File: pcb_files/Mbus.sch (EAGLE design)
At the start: 50 parts, among them IC1 NCP1117ST50T3G, IC3 ATMEGA2560-16AU, IC4 RTC_PCF8523T, J1 F-1X18-SIP-100-32Y, J2 USB_A_SMT_FEMALE, J3 USB_A_SMT_FEMALE, J4 USB_A_SMT_FEMALE, M1 SERVO, Q2 32.768, Y1 CSTCE16M0V53-R0 16MHZ

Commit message: Add resisters for 5V microcontroller to 3.3V pi pin header
Signed-off-by: AlonsoChate <alonsochate@sjtu.edu.cn>
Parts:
- added R2: 3.3k, SmartPrj:R-EU_R0603
- added R3: 1.6k, SmartPrj:R-EU_R0603
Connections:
- net GND: now also R2.1
- net TXD2: now also R2.2, R3.1, R3.2
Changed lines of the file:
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@@
 <drawing>
 <settings>
-<setting alwaysvectorfont="no"/>
+<setting alwaysvectorfont="yes"/>
 <setting verticaltext="up"/>
 </settings>
@@
 <part name="J3" library="SparkFun-Connectors" deviceset="USB_A" device="_SMT_FEMALE"/>
 <part name="J4" library="SparkFun-Connectors" deviceset="USB_A" device="_SMT_FEMALE"/>
+<part name="R2" library="SmartPrj" deviceset="R-EU_" device="R0603" value="3.3k"/>
+<part name="R3" library="SmartPrj" deviceset="R-EU_" device="R0603" value="1.6k"/>
+<part name="GND27" library="supply1" deviceset="GND" device=""/>
 </parts>
 <sheets>
@@
 <instance part="R5" gate="G$1" x="274.32" y="10.16" smashed="yes" rot="R270">
 <attribute name="NAME" x="276.86" y="10.16" size="1.27" layer="95" font="vector" rot="R270" align="center"/>
-<attribute name="VALUE" x="274.32" y="10.16" size="1.016" layer="96" font="vector" ratio="15" rot="R270" align="center"/>
 </instance>
 <instance part="R6" gate="G$1" x="266.7" y="10.16" smashed="yes" rot="R90">
@@
 <attribute name="NAME" x="10.16" y="132.334" size="1.778" layer="95" font="vector" rot="MR0"/>
 <attribute name="VALUE" x="10.16" y="114.554" size="1.778" layer="96" font="vector" rot="R180" align="top-left"/>
+</instance>
+<instance part="R2" gate="G$1" x="320.04" y="83.82" smashed="yes" rot="R90">
+<attribute name="NAME" x="317.5" y="88.0364" size="1.778" layer="95" rot="R180"/>
+<attribute name="VALUE" x="318.135" y="83.312" size="1.778" layer="96" rot="R180"/>
+</instance>
+<instance part="R3" gate="G$1" x="330.2" y="91.44" smashed="yes" rot="R180">
+<attribute name="NAME" x="327.66" y="87.2236" size="1.778" layer="95"/>
+<attribute name="VALUE" x="334.645" y="86.868" size="1.778" layer="96"/>
+</instance>
+<instance part="GND27" gate="1" x="320.04" y="73.66" smashed="yes">
+<attribute name="VALUE" x="317.5" y="71.12" size="1.778" layer="96"/>
 </instance>
 </instances>
@@
 <pinref part="GND11" gate="1" pin="GND"/>
 <wire x1="271.78" y1="76.2" x2="264.16" y2="76.2" width="0.1524" layer="91"/>
+</segment>
+<segment>
+<pinref part="R2" gate="G$1" pin="1"/>
+<pinref part="GND27" gate="1" pin="GND"/>
+<wire x1="320.04" y1="78.74" x2="320.04" y2="76.2" width="0.1524" layer="91"/>
 </segment>
 </net>
@@
 <segment>
 <pinref part="PIHEADER" gate="G$1" pin="RXI/GP15"/>
-<wire x1="302.26" y1="91.44" x2="309.88" y2="91.44" width="0.1524" layer="91"/>
-<label x="304.8" y="91.44" size="1.778" layer="95"/>
-</segment>
-</net>
+<pinref part="R3" gate="G$1" pin="2"/>
+<wire x1="302.26" y1="91.44" x2="320.04" y2="91.44" width="0.1524" layer="91"/>
+<pinref part="R2" gate="G$1" pin="2"/>
+<wire x1="320.04" y1="91.44" x2="325.12" y2="91.44" width="0.1524" layer="91"/>
+<wire x1="320.04" y1="88.9" x2="320.04" y2="91.44" width="0.1524" layer="91"/>
+<junction x="320.04" y="91.44"/>
+</segment>
+<segment>
+<pinref part="R3" gate="G$1" pin="1"/>
+<wire x1="335.28" y1="91.44" x2="340.36" y2="91.44" width="0.1524" layer="91"/>
+<label x="342.9" y="91.44" size="1.778" layer="95"/>
+</segment>
+</net>

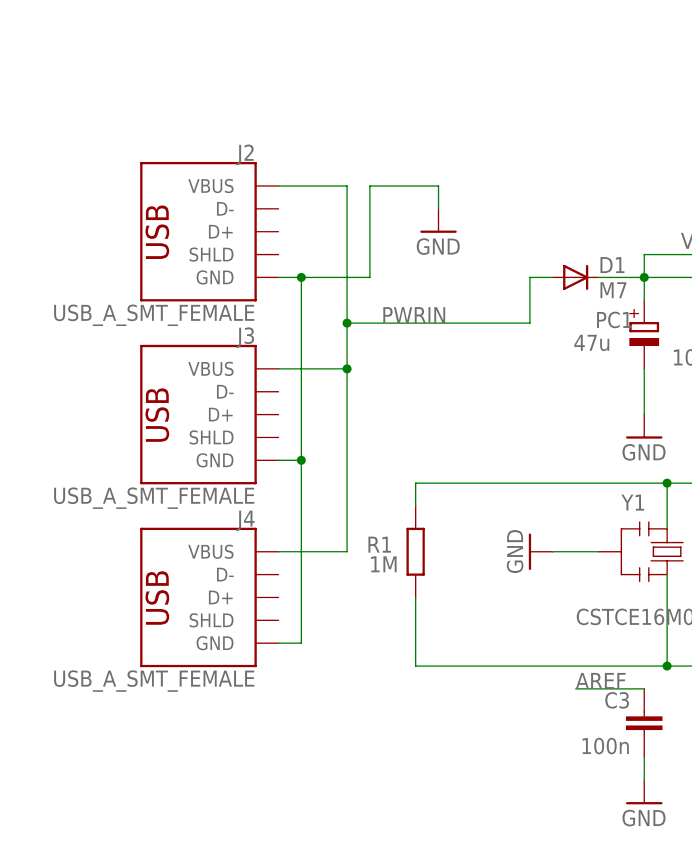
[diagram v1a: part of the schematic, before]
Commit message: modify USB micro-B as power in and USB A port as output
Signed-off-by: Yiteng Cai <alonsochate@umich.edu>
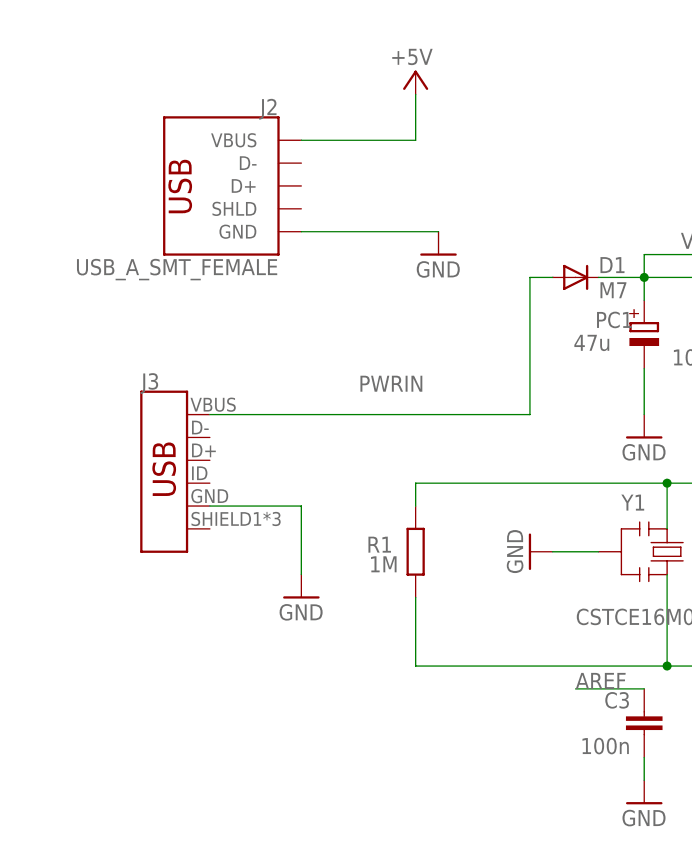
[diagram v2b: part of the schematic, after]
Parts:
- removed J4: USB_A_SMT_FEMALE, SparkFun-Connectors:USB_A_SMT_FEMALE
- J3: value USB_A_SMT_FEMALE -> (none); device SparkFun-Connectors:USB_A_SMT_FEMALE -> SparkFun-Connectors:USB_MICRO-B_FEMALE-SMT
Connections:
- net +5V: now also J2.VBUS
- net GND: no longer J4.GND
- net PWRIN: no longer J2.VBUS, J4.VBUS
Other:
- moved on the sheet: J2
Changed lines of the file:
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@@
 <part name="GND26" library="supply1" library_urn="urn:adsk.eagle:library:371" deviceset="GND" device=""/>
 <part name="J2" library="SparkFun-Connectors" deviceset="USB_A" device="_SMT_FEMALE"/>
-<part name="J3" library="SparkFun-Connectors" deviceset="USB_A" device="_SMT_FEMALE"/>
-<part name="J4" library="SparkFun-Connectors" deviceset="USB_A" device="_SMT_FEMALE"/>
 <part name="R2" library="SmartPrj" deviceset="R-EU_" device="R0603" value="3.3k"/>
 <part name="R3" library="SmartPrj" deviceset="R-EU_" device="R0603" value="1.6k"/>
 <part name="GND27" library="supply1" deviceset="GND" device=""/>
+<part name="J3" library="SparkFun-Connectors" deviceset="USB_MICRO-B" device="_FEMALE-SMT"/>
+<part name="GND28" library="supply1" library_urn="urn:adsk.eagle:library:371" deviceset="GND" device=""/>
+<part name="P+13" library="supply1" deviceset="+5V" device=""/>
 </parts>
 <sheets>
@@
 <attribute name="VALUE" x="83.82" y="86.36" size="1.778" layer="96"/>
 </instance>
-<instance part="GND19" gate="1" x="30.48" y="165.1" smashed="yes">
-<attribute name="VALUE" x="27.94" y="162.56" size="1.778" layer="96"/>
+<instance part="GND19" gate="1" x="30.48" y="162.56" smashed="yes">
+<attribute name="VALUE" x="27.94" y="160.02" size="1.778" layer="96"/>
 </instance>
 <instance part="GND24" gate="1" x="96.52" y="88.9" smashed="yes">
@@
 <attribute name="VALUE" x="236.22" y="22.86" size="1.778" layer="96"/>
 </instance>
-<instance part="J2" gate="G$1" x="5.08" y="165.1" smashed="yes" rot="MR0">
-<attribute name="NAME" x="10.16" y="172.974" size="1.778" layer="95" font="vector" rot="MR0"/>
-<attribute name="VALUE" x="10.16" y="155.194" size="1.778" layer="96" font="vector" rot="R180" align="top-left"/>
-</instance>
-<instance part="J3" gate="G$1" x="5.08" y="144.78" smashed="yes" rot="MR0">
-<attribute name="NAME" x="10.16" y="152.654" size="1.778" layer="95" font="vector" rot="MR0"/>
-<attribute name="VALUE" x="10.16" y="134.874" size="1.778" layer="96" font="vector" rot="R180" align="top-left"/>
-</instance>
-<instance part="J4" gate="G$1" x="5.08" y="124.46" smashed="yes" rot="MR0">
-<attribute name="NAME" x="10.16" y="132.334" size="1.778" layer="95" font="vector" rot="MR0"/>
-<attribute name="VALUE" x="10.16" y="114.554" size="1.778" layer="96" font="vector" rot="R180" align="top-left"/>
+<instance part="J2" gate="G$1" x="7.62" y="170.18" smashed="yes" rot="MR0">
+<attribute name="NAME" x="12.7" y="178.054" size="1.778" layer="95" font="vector" rot="MR0"/>
+<attribute name="VALUE" x="12.7" y="160.274" size="1.778" layer="96" font="vector" rot="R180" align="top-left"/>
 </instance>
 <instance part="R2" gate="G$1" x="320.04" y="83.82" smashed="yes" rot="R90">
@@
 <instance part="GND27" gate="1" x="320.04" y="73.66" smashed="yes">
 <attribute name="VALUE" x="317.5" y="71.12" size="1.778" layer="96"/>
+</instance>
+<instance part="J3" gate="J1" x="0" y="137.16" smashed="yes">
+<attribute name="VALUE" x="-2.54" y="127.254" size="1.778" layer="96" font="vector" rot="MR180" align="top-left"/>
+<attribute name="NAME" x="-2.54" y="147.574" size="1.778" layer="95" font="vector"/>
+</instance>
+<instance part="GND28" gate="1" x="15.24" y="124.46" smashed="yes">
+<attribute name="VALUE" x="12.7" y="121.92" size="1.778" layer="96"/>
+</instance>
+<instance part="P+13" gate="1" x="27.94" y="182.88" smashed="yes">
+<attribute name="VALUE" x="29.845" y="185.42" size="1.778" layer="96" rot="R180"/>
 </instance>
 </instances>
@@
 <wire x1="38.1" y1="12.7" x2="27.94" y2="12.7" width="0.1524" layer="91"/>
 <pinref part="P+19" gate="1" pin="+5V"/>
+</segment>
+<segment>
+<pinref part="P+13" gate="1" pin="+5V"/>
+<wire x1="27.94" y1="180.34" x2="27.94" y2="175.26" width="0.1524" layer="91"/>
+<pinref part="J2" gate="G$1" pin="VBUS"/>
+<wire x1="27.94" y1="175.26" x2="15.24" y2="175.26" width="0.1524" layer="91"/>
 </segment>
 </net>
@@
 </segment>
 <segment>
-<wire x1="22.86" y1="160.02" x2="22.86" y2="170.18" width="0.1524" layer="91"/>
-<pinref part="GND19" gate="1" pin="GND"/>
-<wire x1="22.86" y1="170.18" x2="30.48" y2="170.18" width="0.1524" layer="91"/>
-<wire x1="30.48" y1="170.18" x2="30.48" y2="167.64" width="0.1524" layer="91"/>
-<pinref part="J2" gate="G$1" pin="GND"/>
-<wire x1="12.7" y1="160.02" x2="15.24" y2="160.02" width="0.1524" layer="91"/>
-<pinref part="J3" gate="G$1" pin="GND"/>
-<wire x1="15.24" y1="160.02" x2="22.86" y2="160.02" width="0.1524" layer="91"/>
-<wire x1="12.7" y1="139.7" x2="15.24" y2="139.7" width="0.1524" layer="91"/>
-<wire x1="15.24" y1="139.7" x2="15.24" y2="160.02" width="0.1524" layer="91"/>
-<junction x="15.24" y="160.02"/>
-<pinref part="J4" gate="G$1" pin="GND"/>
-<wire x1="12.7" y1="119.38" x2="15.24" y2="119.38" width="0.1524" layer="91"/>
-<wire x1="15.24" y1="119.38" x2="15.24" y2="139.7" width="0.1524" layer="91"/>
-<junction x="15.24" y="139.7"/>
-</segment>
-<segment>
 <pinref part="PIHEADER" gate="G$1" pin="GND"/>
 <pinref part="GND11" gate="1" pin="GND"/>
@@
 <pinref part="GND27" gate="1" pin="GND"/>
 <wire x1="320.04" y1="78.74" x2="320.04" y2="76.2" width="0.1524" layer="91"/>
+</segment>
+<segment>
+<pinref part="J3" gate="J1" pin="GND"/>
+<wire x1="5.08" y1="134.62" x2="15.24" y2="134.62" width="0.1524" layer="91"/>
+<pinref part="GND28" gate="1" pin="GND"/>
+<wire x1="15.24" y1="134.62" x2="15.24" y2="127" width="0.1524" layer="91"/>
+</segment>
+<segment>
+<pinref part="J2" gate="G$1" pin="GND"/>
+<pinref part="GND19" gate="1" pin="GND"/>
+<wire x1="15.24" y1="165.1" x2="30.48" y2="165.1" width="0.1524" layer="91"/>
 </segment>
 </net>
@@
 <segment>
 <wire x1="40.64" y1="160.02" x2="43.18" y2="160.02" width="0.1524" layer="91"/>
-<wire x1="20.32" y1="154.94" x2="40.64" y2="154.94" width="0.1524" layer="91"/>
-<wire x1="40.64" y1="154.94" x2="40.64" y2="160.02" width="0.1524" layer="91"/>
-<label x="24.13" y="154.94" size="1.778" layer="95"/>
+<wire x1="40.64" y1="144.78" x2="40.64" y2="160.02" width="0.1524" layer="91"/>
+<label x="21.59" y="147.32" size="1.778" layer="95"/>
 <pinref part="D1" gate="G$1" pin="A"/>
-<pinref part="J2" gate="G$1" pin="VBUS"/>
-<wire x1="12.7" y1="170.18" x2="20.32" y2="170.18" width="0.1524" layer="91"/>
-<wire x1="20.32" y1="170.18" x2="20.32" y2="154.94" width="0.1524" layer="91"/>
-<pinref part="J3" gate="G$1" pin="VBUS"/>
-<wire x1="12.7" y1="149.86" x2="20.32" y2="149.86" width="0.1524" layer="91"/>
-<wire x1="20.32" y1="149.86" x2="20.32" y2="154.94" width="0.1524" layer="91"/>
-<junction x="20.32" y="154.94"/>
-<pinref part="J4" gate="G$1" pin="VBUS"/>
-<wire x1="12.7" y1="129.54" x2="20.32" y2="129.54" width="0.1524" layer="91"/>
-<wire x1="20.32" y1="129.54" x2="20.32" y2="149.86" width="0.1524" layer="91"/>
-<junction x="20.32" y="149.86"/>
+<wire x1="40.64" y1="144.78" x2="5.08" y2="144.78" width="0.1524" layer="91"/>
+<pinref part="J3" gate="J1" pin="VBUS"/>
 </segment>
 </net>

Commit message: gpio re-organize
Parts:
- removed C10: 10uF, microbuilder:CAP_CERAMIC0805-NOOUTLINE
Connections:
- new net PD5: IC3.(XCK1)PD5, TESTPIN.6
- new net PD6: IC3.(T1)PD6, TESTPIN.7
- new net PD7: IC3.(T0)PD7, TESTPIN.8
- new net PJ2: IC3.PJ2(XCK3/PCINT11), J1.5
- new net RXD3: IC3.PJ0(RXD3/PCINT9), J1.7
- new net TXD3: IC3.PJ1(TXD3/PCINT10), J1.6
- net +5V: no longer C10.1, IC3.VCC3
- net GND: no longer C10.2, IC3.GND3
- net PB3: no longer TESTPIN.5
- net PB4: no longer TESTPIN.6
- net PB5: no longer TESTPIN.7
- net PB6: no longer TESTPIN.8
- net PD4: now also TESTPIN.5; no longer J1.5
- net RXD0: now also PIHEADER.TXO/GP14; no longer TESTPIN.4
- net RXD1: now also TESTPIN.4; no longer J1.7
- net RXD2: no longer PIHEADER.TXO/GP14
- net SCL: now also TESTPIN.1; no longer TESTPIN.2
- net SDA: now also TESTPIN.2; no longer TESTPIN.1
- net TXD0: now also R3.1; no longer TESTPIN.3
- net TXD1: now also TESTPIN.3; no longer J1.6
- net TXD2: no longer R3.1

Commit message: route update
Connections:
- removed net PJ2: IC3.PJ2(XCK3/PCINT11), J1.5
- net PD7: now also J1.5
- net RXD3: no longer IC3.PJ0(RXD3/PCINT9)
- net TXD3: no longer IC3.PJ1(TXD3/PCINT10)
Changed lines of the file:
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@@
 <pinref part="J1" gate="G$1" pin="6"/>
-</segment>
-<segment>
-<pinref part="IC3" gate="1" pin="PJ1(TXD3/PCINT10)"/>
-<wire x1="104.14" y1="12.7" x2="91.44" y2="12.7" width="0.1524" layer="91"/>
-<label x="96.52" y="12.7" size="1.778" layer="95"/>
 </segment>
 </net>
@@
 <label x="203.2" y="-2.54" size="1.778" layer="95"/>
 <pinref part="J1" gate="G$1" pin="7"/>
-</segment>
-<segment>
-<pinref part="IC3" gate="1" pin="PJ0(RXD3/PCINT9)"/>
-<wire x1="104.14" y1="10.16" x2="91.44" y2="10.16" width="0.1524" layer="91"/>
-<label x="96.52" y="10.16" size="1.778" layer="95"/>
-</segment>
-</net>
-<net name="PJ2" class="0">
-<segment>
-<wire x1="213.36" y1="2.54" x2="200.66" y2="2.54" width="0.1524" layer="91"/>
-<label x="203.2" y="2.54" size="1.778" layer="95"/>
-<pinref part="J1" gate="G$1" pin="5"/>
-</segment>
-<segment>
-<pinref part="IC3" gate="1" pin="PJ2(XCK3/PCINT11)"/>
-<wire x1="104.14" y1="15.24" x2="91.44" y2="15.24" width="0.1524" layer="91"/>
-<label x="96.52" y="15.24" size="1.778" layer="95"/>
 </segment>
 </net>
@@
 <label x="180.34" y="68.58" size="1.778" layer="95"/>
 </segment>
+<segment>
+<wire x1="213.36" y1="2.54" x2="200.66" y2="2.54" width="0.1524" layer="91"/>
+<label x="203.2" y="2.54" size="1.778" layer="95"/>
+<pinref part="J1" gate="G$1" pin="5"/>
+</segment>
 </net>
